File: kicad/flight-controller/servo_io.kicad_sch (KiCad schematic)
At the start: 1 part, among them J7 RC Connector

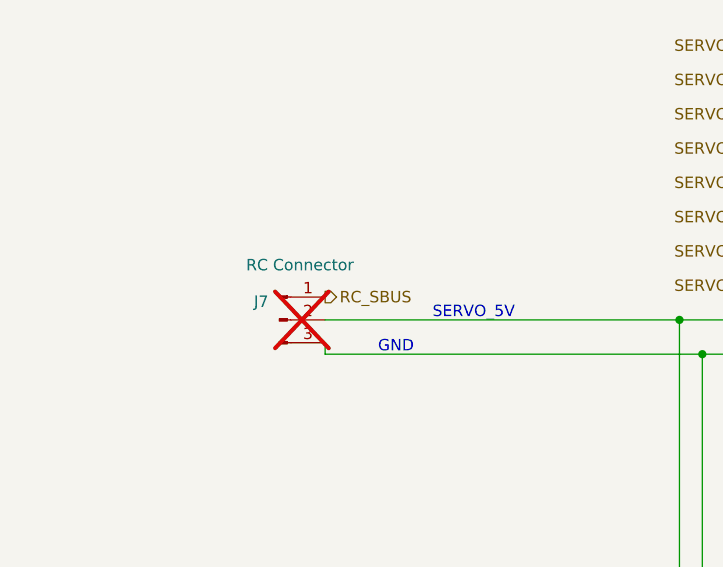
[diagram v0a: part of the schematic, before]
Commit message: Fix ESP32 LDO thermal margin, add USB-C/SBUS ESD protection
Design review flagged the ESP32-S3's 3.3V LDO (AP2112K-3.3, SOT-23-5)
at only 1.5C margin to absolute max under WiFi load. Swapped to a
Torex XC6220B331PR-G (SOT-89-5, thermal tab tied to GND) with matching
input/output caps and thermal vias under the tab; thermal score is now
100/100 with no findings. Sensor LDO (U6) was unaffected and left as-is.

Also added TVS protection that was missing on two exposed signal paths:
D4 + bulk cap on USB-C VBUS (J13, now populated for field use) ahead of
the existing blocking diode, and a matching TVS (D6) on the RC receiver
SBUS line (J7), reusing the same part to minimize BOM diversity.

Every part number touched this pass (U4, C17-C19, D4, D6) was verified
against real distributor data, and a full BOM audit confirmed all other
assigned part numbers match their stated value and footprint. Also
removed two orphaned, unwired schematic files (airspeed.kicad_sch,
lidar.kicad_sch) that weren't in the sheet hierarchy.

Known follow-up before fab: the production/ fab package predates this
rework and needs to be regenerated, and Update PCB from Schematic needs
a re-run to sync D4/D6's display value (nets are already correct).

Co-Authored-By: Claude Sonnet 5 <noreply@anthropic.com>
Claude-Session: https://claude.ai/code/session_01NksRnW4jXLWsYwZNR7u39H
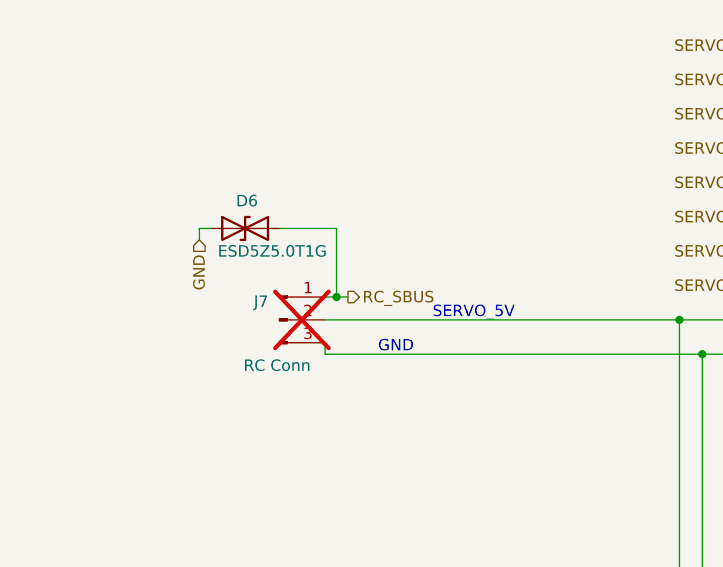
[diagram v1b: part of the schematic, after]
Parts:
- added D6: ESD5Z5.0T1G, Diode_SMD:D_SOD-523, symbol Device:D_TVS
- J7: value RC Connector -> RC Conn
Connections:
- net GND: now also D6.1 (A1)
- net RC_SBUS: now also D6.2 (A2)
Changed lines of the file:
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@@
 		(title "Actuator IO")
 		(date "2026-09-09")
-		(rev "v3.0")
+		(rev "v3.1")
 		(company "Travis Brown")
 	)
@@
 	)
 	(junction
+		(at 100.33 86.36)
+		(diameter 0)
+		(color 0 0 0 0)
+	)
+	(junction
 		(at 125.73 135.89)
 		(diameter 0)
@@
 	(wire
 		(pts
+			(xy 100.33 78.74) (xy 100.33 86.36)
+		)
+		(stroke
+			(width 0)
+			(type default)
+		)
+	)
+	(wire
+		(pts
 			(xy 140.97 135.89) (xy 140.97 92.71)
 		)
@@
 	(wire
 		(pts
+			(xy 93.98 78.74) (xy 100.33 78.74)
+		)
+		(stroke
+			(width 0)
+			(type default)
+		)
+	)
+	(wire
+		(pts
 			(xy 118.11 128.27) (xy 125.73 128.27)
 		)
@@
 	(wire
 		(pts
+			(xy 100.33 86.36) (xy 101.6 86.36)
+		)
+		(stroke
+			(width 0)
+			(type default)
+		)
+	)
+	(wire
+		(pts
+			(xy 85.09 78.74) (xy 86.36 78.74)
+		)
+		(stroke
+			(width 0)
+			(type default)
+		)
+	)
+	(wire
+		(pts
+			(xy 99.06 86.36) (xy 100.33 86.36)
+		)
+		(stroke
+			(width 0)
+			(type default)
+		)
+	)
+	(wire
+		(pts
 			(xy 118.11 132.08) (xy 138.43 132.08)
 		)
@@
 		)
 	)
+	(wire
+		(pts
+			(xy 85.09 78.74) (xy 85.09 80.01)
+		)
+		(stroke
+			(width 0)
+			(type default)
+		)
+	)
 	(hierarchical_label "ESC_OUT2"
 		(shape input)
 		(at 77.47 133.35 180)
+		(effects
+			(font
+				(size 1.27 1.27)
+			)
+			(justify right)
+		)
+	)
+	(hierarchical_label "GND"
+		(shape input)
+		(at 85.09 80.01 270)
 		(effects
 			(font
@@
 		)
 	)
+	(hierarchical_label "SERVO_OUT5"
+		(shape input)
+		(at 151.13 73.66 180)
+		(effects
+			(font
+				(size 1.27 1.27)
+			)
+			(justify right)
+		)
+	)
+	(hierarchical_label "SERVO_OUT7"
+		(shape input)
+		(at 151.13 81.28 180)
+		(effects
+			(font
+				(size 1.27 1.27)
+			)
+			(justify right)
+		)
+	)
 	(hierarchical_label "RC_SBUS"
 		(shape output)
-		(at 99.06 86.36 0)
+		(at 101.6 86.36 0)
 		(effects
 			(font
@@
 			)
 			(justify left)
-		)
-	)
-	(hierarchical_label "SERVO_OUT5"
-		(shape input)
-		(at 151.13 73.66 180)
-		(effects
-			(font
-				(size 1.27 1.27)
-			)
-			(justify right)
-		)
-	)
-	(hierarchical_label "SERVO_OUT7"
-		(shape input)
-		(at 151.13 81.28 180)
-		(effects
-			(font
-				(size 1.27 1.27)
-			)
-			(justify right)
 		)
 	)
@@
 			)
 		)
-		(property "Value" "RC Connector"
-			(at 96.266 82.804 0)
+		(property "Value" "RC Conn"
+			(at 93.726 93.98 0)
 			(show_name no)
 			(do_not_autoplace no)
@@
 					(unit 1)
 				)
+			)
+		)
+	)
+	(symbol
+		(lib_id "Device:D_TVS")
+		(at 90.17 78.74 0)
+		(unit 1)
+		(body_style 1)
+		(exclude_from_sim no)
+		(in_bom yes)
+		(on_board yes)
+		(in_pos_files yes)
+		(dnp no)
+		(property "Reference" "D6"
+			(at 89.154 75.692 0)
+			(show_name no)
+			(do_not_autoplace no)
+			(effects
+				(font
+					(size 1.27 1.27)
+				)
+				(justify left)
+			)
+		)
+		(property "Value" "ESD5Z5.0T1G"
+			(at 87.122 81.28 0)
+			(show_name no)
+			(do_not_autoplace no)
+			(effects
+				(font
+					(size 1.27 1.27)
+				)
+				(justify left)
+			)
+		)
+		(property "Footprint" "Diode_SMD:D_SOD-523"
+			(at 90.17 78.74 0)
+			(hide yes)
+			(show_name no)
+			(do_not_autoplace no)
+			(effects
+				(font
+					(size 1.27 1.27)
+				)
+			)
+		)
+		(property "Datasheet" "https://www.lcsc.com/datasheet/C82044.pdf"
+			(at 90.17 78.74 0)
+			(hide yes)
+			(show_name no)
+			(do_not_autoplace no)
+			(effects
+				(font
+					(size 1.27 1.27)
+				)
+			)
+		)
+		(property "Description" "TVS diode, onsemi, 5V standoff / 6.2V breakdown, unidirectional"
+			(at 90.17 78.74 0)
+			(hide yes)
+			(show_name no)
+			(do_not_autoplace no)
+			(effects
+				(font
+					(size 1.27 1.27)
+				)
+			)
+		)
+		(property "Notes" "SBUS signal ESD/surge protection (added in review)"
+			(at 90.17 78.74 0)
+			(hide yes)
+			(show_name no)
+			(do_not_autoplace no)
+			(effects
+				(font
+					(size 1.27 1.27)
+				)
+			)
+		)
+		(property "LCSC Part" "C82044"
+			(at 90.17 78.74 0)
+			(hide yes)
+			(show_name no)
+			(do_not_autoplace no)
+			(effects
+				(font
+					(size 1.27 1.27)
+				)
+			)
+		)
+		(pin "1"
+		)
+		(pin "2"
+		)
+		(instances
+			(project "fixed-wing-drone"
+				(path "/6fbedc8c-8b3e-4075-8dcf-52085fc3223b/c5f0c20f-db19-4cbe-9f5c-05ea41a374c0"
+					(reference "D6")
+					(unit 1)
+				)
